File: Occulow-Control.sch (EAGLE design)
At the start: 27 parts, among them J1 CORTEX_DEBUG_PTH, T1 DMP3010LK3, T2 DMP3010LK3, T3 DMP3010LK3

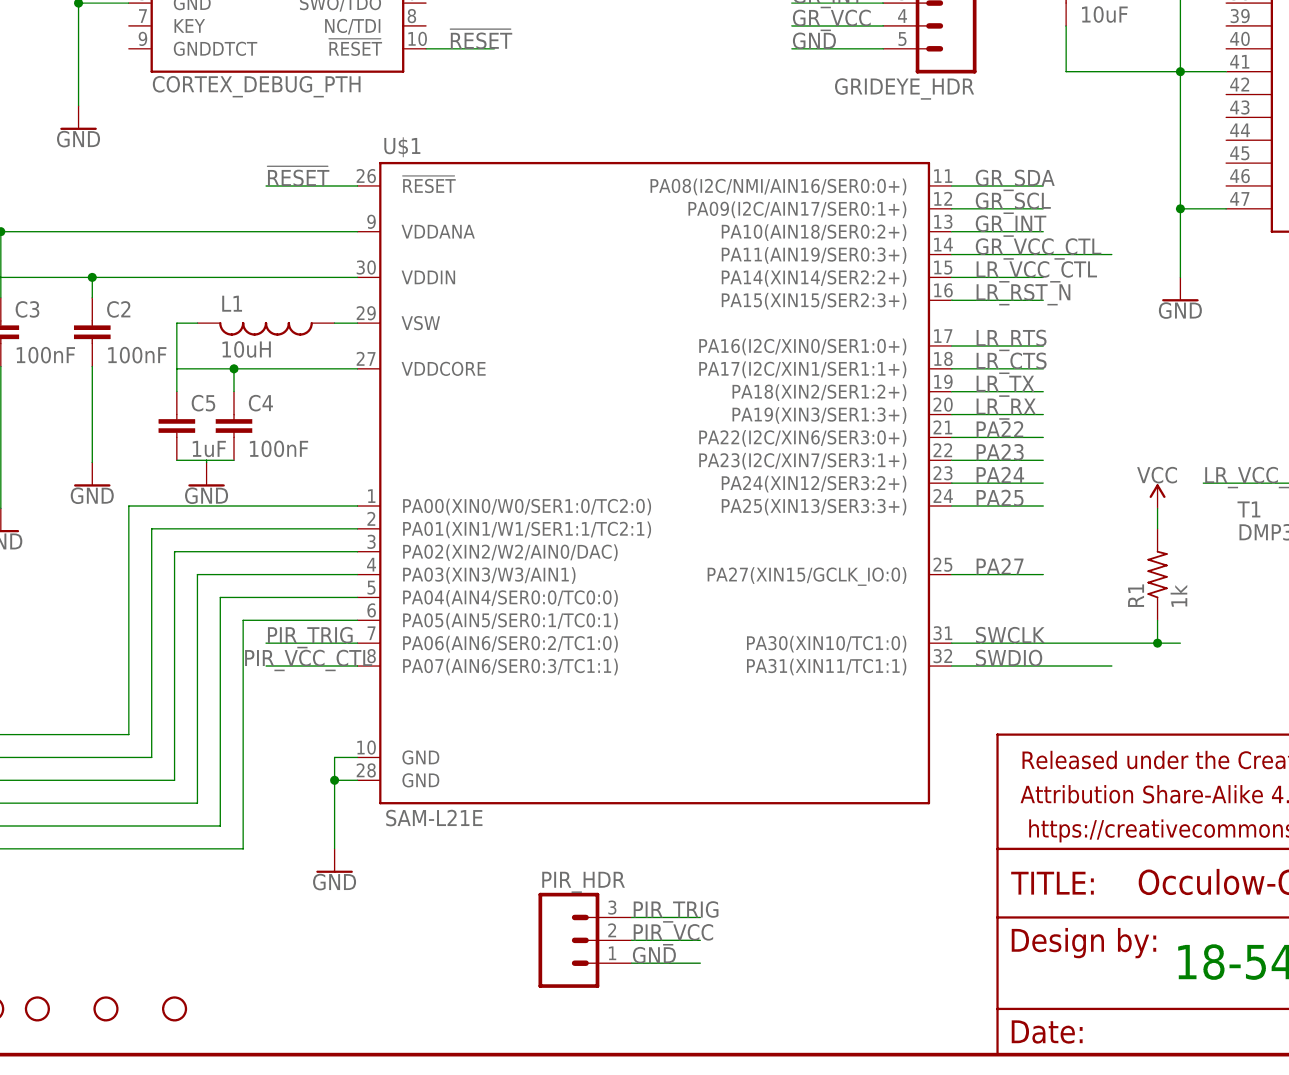
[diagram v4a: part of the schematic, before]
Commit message: Grideye, PIR, most power routing
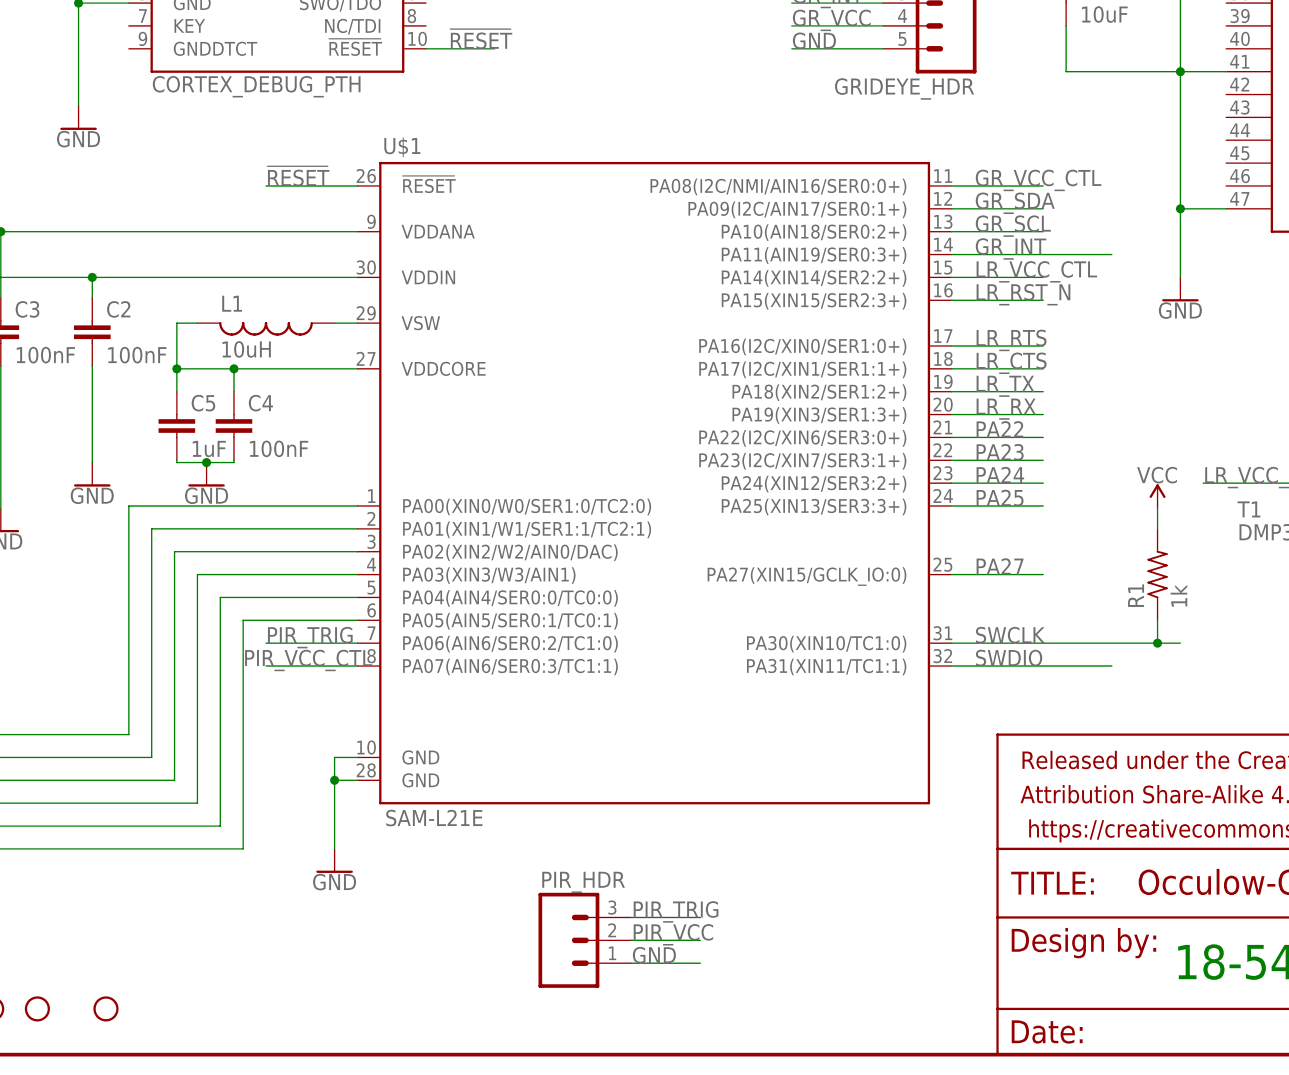
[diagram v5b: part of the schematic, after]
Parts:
- removed H4: STAND-OFF, SparkFun-Hardware:STAND-OFF
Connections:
- net GR_INT: now also U$1.PA11(AIN19/SER0:3+); no longer U$1.PA10(AIN18/SER0:2+)
- net GR_SCL: now also U$1.PA10(AIN18/SER0:2+); no longer U$1.PA09(I2C/AIN17/SER0:1+)
- net GR_SDA: now also U$1.PA09(I2C/AIN17/SER0:1+); no longer U$1.PA08(I2C/NMI/AIN16/SER0:0+)
- net GR_VCC_CTL: now also U$1.PA08(I2C/NMI/AIN16/SER0:0+); no longer U$1.PA11(AIN19/SER0:3+)
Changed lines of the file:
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@@
 <part name="H2" library="SparkFun-Hardware" deviceset="STAND-OFF" device=""/>
 <part name="H3" library="SparkFun-Hardware" deviceset="STAND-OFF" device=""/>
-<part name="H4" library="SparkFun-Hardware" deviceset="STAND-OFF" device=""/>
 </parts>
 <sheets>
@@
 <instance part="H2" gate="G$1" x="40.64" y="5.08"/>
 <instance part="H3" gate="G$1" x="48.26" y="5.08"/>
-<instance part="H4" gate="G$1" x="55.88" y="5.08"/>
 </instances>
 <busses>
@@
 </segment>
 <segment>
-<pinref part="C5" gate="G$1" pin="2"/>
-<pinref part="GND4" gate="1" pin="GND"/>
-<wire x1="56.134" y1="66.04" x2="59.436" y2="66.04" width="0.1524" layer="91"/>
-<pinref part="C4" gate="G$1" pin="2"/>
-<wire x1="62.484" y1="66.04" x2="59.436" y2="66.04" width="0.1524" layer="91"/>
-<wire x1="59.436" y1="66.04" x2="59.436" y2="65.786" width="0.1524" layer="91"/>
-</segment>
-<segment>
 <pinref part="C2" gate="G$1" pin="2"/>
 <pinref part="GND13" gate="1" pin="GND"/>
@@
 <wire x1="134.62" y1="139.7" x2="116.84" y2="139.7" width="0.1524" layer="91"/>
 <wire x1="116.84" y1="139.7" x2="116.84" y2="133.604" width="0.1524" layer="91"/>
+</segment>
+<segment>
+<pinref part="GND4" gate="1" pin="GND"/>
+<pinref part="C4" gate="G$1" pin="2"/>
+<wire x1="59.436" y1="65.786" x2="62.484" y2="65.786" width="0.1524" layer="91"/>
+<wire x1="62.484" y1="65.786" x2="62.484" y2="66.04" width="0.1524" layer="91"/>
+<pinref part="C5" gate="G$1" pin="2"/>
+<wire x1="59.436" y1="65.786" x2="56.134" y2="65.786" width="0.1524" layer="91"/>
+<wire x1="56.134" y1="65.786" x2="56.134" y2="66.04" width="0.1524" layer="91"/>
+<junction x="59.436" y="65.786"/>
 </segment>
 </net>
@@
 <net name="GR_SDA" class="0">
 <segment>
+<pinref part="GRIDEYE_HDR" gate="G$1" pin="1"/>
+<wire x1="134.62" y1="121.92" x2="124.46" y2="121.92" width="0.1524" layer="91"/>
+<label x="124.46" y="121.92" size="1.778" layer="95"/>
+</segment>
+<segment>
+<pinref part="U$1" gate="G$1" pin="PA09(I2C/AIN17/SER0:1+)"/>
+<wire x1="142.24" y1="93.98" x2="152.4" y2="93.98" width="0.1524" layer="91"/>
+<label x="144.78" y="93.98" size="1.778" layer="95"/>
+</segment>
+</net>
+<net name="GR_SCL" class="0">
+<segment>
+<pinref part="GRIDEYE_HDR" gate="G$1" pin="2"/>
+<wire x1="134.62" y1="119.38" x2="124.46" y2="119.38" width="0.1524" layer="91"/>
+<label x="124.46" y="119.38" size="1.778" layer="95"/>
+</segment>
+<segment>
+<pinref part="U$1" gate="G$1" pin="PA10(AIN18/SER0:2+)"/>
+<wire x1="142.24" y1="91.44" x2="152.4" y2="91.44" width="0.1524" layer="91"/>
+<label x="144.78" y="91.44" size="1.778" layer="95"/>
+</segment>
+</net>
+<net name="GR_INT" class="0">
+<segment>
+<pinref part="GRIDEYE_HDR" gate="G$1" pin="3"/>
+<wire x1="134.62" y1="116.84" x2="124.46" y2="116.84" width="0.1524" layer="91"/>
+<label x="124.46" y="116.84" size="1.778" layer="95"/>
+</segment>
+<segment>
+<pinref part="U$1" gate="G$1" pin="PA11(AIN19/SER0:3+)"/>
+<label x="144.78" y="88.9" size="1.778" layer="95"/>
+<wire x1="160.02" y1="88.9" x2="142.24" y2="88.9" width="0.1524" layer="91"/>
+</segment>
+</net>
+<net name="GR_VCC_CTL" class="0">
+<segment>
+<pinref part="T2" gate="G$1" pin="G"/>
+<wire x1="210.82" y1="63.5" x2="195.58" y2="63.5" width="0.1524" layer="91"/>
+<label x="195.58" y="63.5" size="1.778" layer="95"/>
+</segment>
+<segment>
 <pinref part="U$1" gate="G$1" pin="PA08(I2C/NMI/AIN16/SER0:0+)"/>
 <wire x1="142.24" y1="96.52" x2="152.4" y2="96.52" width="0.1524" layer="91"/>
 <label x="144.78" y="96.52" size="1.778" layer="95"/>
-</segment>
-<segment>
-<pinref part="GRIDEYE_HDR" gate="G$1" pin="1"/>
-<wire x1="134.62" y1="121.92" x2="124.46" y2="121.92" width="0.1524" layer="91"/>
-<label x="124.46" y="121.92" size="1.778" layer="95"/>
-</segment>
-</net>
-<net name="GR_SCL" class="0">
-<segment>
-<pinref part="U$1" gate="G$1" pin="PA09(I2C/AIN17/SER0:1+)"/>
-<wire x1="142.24" y1="93.98" x2="152.4" y2="93.98" width="0.1524" layer="91"/>
-<label x="144.78" y="93.98" size="1.778" layer="95"/>
-</segment>
-<segment>
-<pinref part="GRIDEYE_HDR" gate="G$1" pin="2"/>
-<wire x1="134.62" y1="119.38" x2="124.46" y2="119.38" width="0.1524" layer="91"/>
-<label x="124.46" y="119.38" size="1.778" layer="95"/>
-</segment>
-</net>
-<net name="GR_INT" class="0">
-<segment>
-<pinref part="U$1" gate="G$1" pin="PA10(AIN18/SER0:2+)"/>
-<wire x1="142.24" y1="91.44" x2="152.4" y2="91.44" width="0.1524" layer="91"/>
-<label x="144.78" y="91.44" size="1.778" layer="95"/>
-</segment>
-<segment>
-<pinref part="GRIDEYE_HDR" gate="G$1" pin="3"/>
-<wire x1="134.62" y1="116.84" x2="124.46" y2="116.84" width="0.1524" layer="91"/>
-<label x="124.46" y="116.84" size="1.778" layer="95"/>
-</segment>
-</net>
-<net name="GR_VCC_CTL" class="0">
-<segment>
-<pinref part="U$1" gate="G$1" pin="PA11(AIN19/SER0:3+)"/>
-<label x="144.78" y="88.9" size="1.778" layer="95"/>
-<wire x1="160.02" y1="88.9" x2="142.24" y2="88.9" width="0.1524" layer="91"/>
-</segment>
-<segment>
-<pinref part="T2" gate="G$1" pin="G"/>
-<wire x1="210.82" y1="63.5" x2="195.58" y2="63.5" width="0.1524" layer="91"/>
-<label x="195.58" y="63.5" size="1.778" layer="95"/>
 </segment>
 </net>
@@
 </segment>
 </net>
+<net name="PA24" class="0">
+<segment>
+<pinref part="U$1" gate="G$1" pin="PA24(XIN12/SER3:2+)"/>
+<wire x1="142.24" y1="63.5" x2="152.4" y2="63.5" width="0.1524" layer="91"/>
+<label x="144.78" y="63.5" size="1.778" layer="95"/>
+</segment>
+<segment>
+<wire x1="134.62" y1="149.86" x2="124.46" y2="149.86" width="0.1524" layer="91"/>
+<label x="124.46" y="149.86" size="1.778" layer="95"/>
+<pinref part="SL1" gate="G$1" pin="3"/>
+</segment>
+</net>
+<net name="PA25" class="0">
+<segment>
+<pinref part="U$1" gate="G$1" pin="PA25(XIN13/SER3:3+)"/>
+<wire x1="142.24" y1="60.96" x2="152.4" y2="60.96" width="0.1524" layer="91"/>
+<label x="144.78" y="60.96" size="1.778" layer="95"/>
+</segment>
+<segment>
+<pinref part="SL1" gate="G$1" pin="4"/>
+<wire x1="134.62" y1="147.32" x2="124.46" y2="147.32" width="0.1524" layer="91"/>
+<label x="124.46" y="147.32" size="1.778" layer="95"/>
+</segment>
+</net>
 <net name="VDDCORE" class="0">
 <segment>
+<pinref part="C5" gate="G$1" pin="1"/>
 <pinref part="L1" gate="G$1" pin="2"/>
-<pinref part="C5" gate="G$1" pin="1"/>
 <wire x1="58.42" y1="81.28" x2="56.134" y2="81.28" width="0.1524" layer="91"/>
 <wire x1="56.134" y1="81.28" x2="56.134" y2="76.2" width="0.1524" layer="91"/>
@@
 <wire x1="56.134" y1="76.2" x2="56.134" y2="73.66" width="0.1524" layer="91"/>
 <wire x1="76.2" y1="76.2" x2="62.484" y2="76.2" width="0.1524" layer="91"/>
+<junction x="56.134" y="76.2"/>
+<pinref part="C4" gate="G$1" pin="1"/>
 <wire x1="62.484" y1="76.2" x2="56.134" y2="76.2" width="0.1524" layer="91"/>
-<pinref part="C4" gate="G$1" pin="1"/>
 <wire x1="62.484" y1="73.66" x2="62.484" y2="76.2" width="0.1524" layer="91"/>
 <junction x="62.484" y="76.2"/>
 </segment>
 </net>
-<net name="PA24" class="0">
-<segment>
-<pinref part="U$1" gate="G$1" pin="PA24(XIN12/SER3:2+)"/>
-<wire x1="142.24" y1="63.5" x2="152.4" y2="63.5" width="0.1524" layer="91"/>
-<label x="144.78" y="63.5" size="1.778" layer="95"/>
-</segment>
-<segment>
-<wire x1="134.62" y1="149.86" x2="124.46" y2="149.86" width="0.1524" layer="91"/>
-<label x="124.46" y="149.86" size="1.778" layer="95"/>
-<pinref part="SL1" gate="G$1" pin="3"/>
-</segment>
-</net>
-<net name="PA25" class="0">
-<segment>
-<pinref part="U$1" gate="G$1" pin="PA25(XIN13/SER3:3+)"/>
-<wire x1="142.24" y1="60.96" x2="152.4" y2="60.96" width="0.1524" layer="91"/>
-<label x="144.78" y="60.96" size="1.778" layer="95"/>
-</segment>
-<segment>
-<pinref part="SL1" gate="G$1" pin="4"/>
-<wire x1="134.62" y1="147.32" x2="124.46" y2="147.32" width="0.1524" layer="91"/>
-<label x="124.46" y="147.32" size="1.778" layer="95"/>
-</segment>
-</net>

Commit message: Changed to breakouts, added sheets
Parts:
- added C10: 1.5 uF, rcl:C-EUC1206
- added C8: 10 uF, rcl:C-EUC1206
- added C9: 1 uF, rcl:C-EUC1206
- added EXTRA_HDR, LR_CTL_HDR, LR_HDR: (no value), con-amp-quick:M07
- added FRAME2, FRAME3: FRAME-LETTERNO_PACKAGE, SparkFun-Aesthetics:FRAME-LETTERNO_PACKAGE
- added R2, R3, R4: 10k, resistor:R-US_R1206
- added R5: 20, resistor:R-US_R1206
- added U$4: AMG8833SMD, GridEye:AMG8833SMD
- SL1: device con-amp-quick:M07 -> con-amp-quick:M05
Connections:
- new net GR_GND: C10.2, C8.2, R5.1, SL1.5, U$4.AD_SELECT, U$4.GND
- new net GR_INT_HDR: GRIDEYE_HDR.3, U$1.PA11(AIN19/SER0:3+)
- new net GR_SCL_HDR: GRIDEYE_HDR.2, U$1.PA10(AIN18/SER0:2+)
- new net GR_SDA_HDR: GRIDEYE_HDR.1, U$1.PA09(I2C/AIN17/SER0:1+)
- new net LR_CTS_HDR: LR_CTL_HDR.3, U$1.PA17(I2C/XIN1/SER1:1+)
- new net LR_GND: C6.2, LR_HDR.1, U$2.GND1, U$2.GND10, U$2.GND11, U$2.GND12, U$2.GND13, U$2.GND2, U$2.GND3, U$2.GND4, U$2.GND5, U$2.GND6, U$2.GND7, U$2.GND8, U$2.GND9, U$3.GND1, U$3.GND2, U$3.GND3, U$3.GND4
- new net LR_RST_N_HDR: LR_CTL_HDR.1, U$1.PA15(XIN15/SER2:3+)
- new net LR_RTS_HDR: LR_CTL_HDR.2, U$1.PA16(I2C/XIN0/SER1:0+)
- new net LR_RX_HDR: LR_CTL_HDR.5, U$1.PA19(XIN3/SER1:3+)
- new net LR_TX_HDR: LR_CTL_HDR.4, U$1.PA18(XIN2/SER1:2+)
- new net LR_VCC_HDR: LR_CTL_HDR.6, T1.D
- new net N$2: C9.1, U$4.AVDD-PC
- new net N$3: C9.2, R5.2
- new net N$4: C10.1, U$4.DVDD-PC
- net GND: now also EXTRA_HDR.7, LR_CTL_HDR.7; no longer C6.2, SL1.7, U$2.GND1, U$2.GND10, U$2.GND11, U$2.GND12, U$2.GND13, U$2.GND2, U$2.GND3, U$2.GND4, U$2.GND5, U$2.GND6, U$2.GND7, U$2.GND8, U$2.GND9, U$3.GND1, U$3.GND2, U$3.GND3, U$3.GND4
- net GR_INT: now also R2.1, SL1.1, U$4.INT; no longer GRIDEYE_HDR.3, U$1.PA11(AIN19/SER0:3+)
- net GR_SCL: now also R4.1, SL1.2, U$4.SCL; no longer GRIDEYE_HDR.2, U$1.PA10(AIN18/SER0:2+)
- net GR_SDA: now also R3.1, SL1.3, U$4.SDA; no longer GRIDEYE_HDR.1, U$1.PA09(I2C/AIN17/SER0:1+)
- net GR_VCC: now also C8.1, R2.2, R3.2, R4.2, SL1.4, U$4.VDD, U$4.VPP
- net LR_CTS: now also LR_HDR.6; no longer U$1.PA17(I2C/XIN1/SER1:1+)
- net LR_RST_N: now also LR_HDR.3; no longer U$1.PA15(XIN15/SER2:3+)
- net LR_RTS: now also LR_HDR.7; no longer U$1.PA16(I2C/XIN0/SER1:0+)
- net LR_RX: now also LR_HDR.4; no longer U$1.PA19(XIN3/SER1:3+)
- net LR_TX: now also LR_HDR.5; no longer U$1.PA18(XIN2/SER1:2+)
- net LR_VCC: now also LR_HDR.2; no longer T1.D
- net PA22: now also EXTRA_HDR.1; no longer SL1.1
- net PA23: now also EXTRA_HDR.2; no longer SL1.2
- net PA24: now also EXTRA_HDR.3; no longer SL1.3
- net PA25: now also EXTRA_HDR.4; no longer SL1.4
- net PA27: now also EXTRA_HDR.5; no longer SL1.5
- net VCC: now also EXTRA_HDR.6; no longer SL1.6, T1.S, T2.S, T3.S
- net VDDCORE: now also T1.S, T2.S, T3.S
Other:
- note added: "2"
- note removed: "1"
